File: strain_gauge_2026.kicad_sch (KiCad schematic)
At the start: 0 parts

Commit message: Created Strain Gauge Board Schematic version 1
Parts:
- added C1: 0.1u, Package_SO:SOIC-16_3.9x9.9mm_P1.27mm, symbol Device:C
- added C2, C3, C4, C7, C8: 0.1uF, symbol Device:C
- added C5, C6: 10uF, symbol Device:C
- added J2, J3: Conn_01x04_Socket, Package_DFN_QFN:QFN-20-1EP_5x5mm_P0.65mm_EP3.35x3.35mm, symbol Connector:Conn_01x04_Socket
- added JP1: SolderJumper_2_Open, symbol Jumper:SolderJumper_2_Open
- added L1: 3.3uH, symbol Device:L
- added Q1: S8550, Package_TO_SOT_THT:TO-92_Inline, symbol Transistor_BJT:S8550
- added R1: 10k, symbol Device:R
- added R10, R11, R8, R9: 100, symbol Device:R
- added R12: 20k, Package_TO_SOT_THT:TO-92_Inline, symbol Device:R
- added R13: 8.2k, Package_TO_SOT_THT:TO-92_Inline, symbol Device:R
- added R2, R3, R4, R5, R6, R7: 350, symbol Device:R
- added U1: HX711, Package_SO:SOIC-16_3.9x9.9mm_P1.27mm, symbol Analog_ADC:HX711
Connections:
- new net: C3.2, R11.2, U1.9 (INB-)
- new net: L1.2, Q1.3 (C), R12.1, U1.3 (AVDD)
- new net: R12.2, R13.1, U1.4 (VFB)
- new net: C1.1, U1.6 (VBG)
- new net: JP1.2 (B), R1.2, U1.15 (RATE)
- new net: C3.1, R10.2, U1.10 (INB+)
- new net: C2.2, R9.2, U1.7 (INA-)
- new net: Q1.2 (B), U1.2 (BASE)
- new net: C2.1, R8.2, U1.8 (INA+)
- new net +3V3: C6.1, C7.1, C8.1, J2.1 (Pin_1), Q1.1 (E), R1.1, U1.1 (VSUP), U1.16 (DVDD)
- new net A+: J3.1 (Pin_1), R3.1, R8.1
- new net A-: R2.1, R4.2, R9.1
- new net B+: J3.3 (Pin_3), R10.1, R7.1
- new net B-: R11.1, R5.1, R6.2
- new net Data Out: J2.2 (Pin_2), U1.12 (DOUT)
- new net GND: C1.2, C4.2, C5.2, C6.2, C7.2, C8.2, J2.4 (Pin_4), J3.2 (Pin_2), J3.4 (Pin_4), JP1.1 (A), R13.2, R4.1, R6.1, U1.14 (XI), U1.5 (AGND)
- new net SCK: J2.3 (Pin_3), U1.11 (PD_SCK)
- new net V_AVDD: C4.1, C5.1, L1.1, R2.2, R3.2, R5.2, R7.2
- no-connect marks 0 -> 1
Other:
- note added: "Decoupling caps"
- note added: "Figure out if doing a half bridge - 2 strain resistors on opposite side of beam - R3 and R7 would change to strain resistors - compensates for temperature, and is more sensitive"
- note added: "HX711: https://e2e.ti.com/cfs-file/__key/communityserver-discussions-components-files/73/HX711.pdf SparkFun Board: https://cdn.sparkfun.com/assets/f/5/5/b/c/SparkFun_HX711_Load_Cell.pdf"
- note added: "MCU Connections"
- note added: "Purdue Lunabotics HX711 Strain Gauge Amplifier"
- note added: "RATE is 10 Samples/Sec when grounded, 80 Samples/Sec when pulled up"
- note added: "References Used:"
- note added: "September 26th, 2026"
- note added: "Strain Resistor R_nominal = 350"
- note added: "Strain resistor connections"
- note added: "v1"

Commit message: Fixed ERC errors
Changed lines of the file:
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@@
 	)
 	(junction
-		(at 156.21 151.13)
-		(diameter 0)
-		(color 0 0 0 0)
-	)
-	(junction
 		(at 104.14 92.71)
 		(diameter 0)
@@
 	)
 	(junction
-		(at 162.56 140.97)
-		(diameter 0)
-		(color 0 0 0 0)
-	)
-	(junction
 		(at 104.14 53.34)
 		(diameter 0)
@@
 	)
 	(junction
-		(at 113.03 151.13)
-		(diameter 0)
-		(color 0 0 0 0)
-	)
-	(junction
-		(at 119.38 140.97)
+		(at 104.14 87.63)
 		(diameter 0)
 		(color 0 0 0 0)
 	)
 	(junction
-		(at 104.14 87.63)
+		(at 107.95 50.8)
 		(diameter 0)
 		(color 0 0 0 0)
@@
 	(wire
 		(pts
-			(xy 156.21 151.13) (xy 162.56 151.13)
-		)
-		(stroke
-			(width 0)
-			(type default)
-		)
-	)
-	(wire
-		(pts
 			(xy 99.06 80.01) (xy 104.14 80.01)
 		)
@@
 	(wire
 		(pts
-			(xy 119.38 140.97) (xy 119.38 143.51)
-		)
-		(stroke
-			(width 0)
-			(type default)
-		)
-	)
-	(wire
-		(pts
 			(xy 133.35 58.42) (xy 135.89 58.42)
 		)
@@
 	(wire
 		(pts
-			(xy 113.03 151.13) (xy 119.38 151.13)
-		)
-		(stroke
-			(width 0)
-			(type default)
-		)
-	)
-	(wire
-		(pts
 			(xy 87.63 80.01) (xy 91.44 80.01)
 		)
@@
 	(wire
 		(pts
-			(xy 162.56 140.97) (xy 162.56 143.51)
-		)
-		(stroke
-			(width 0)
-			(type default)
-		)
-	)
-	(wire
-		(pts
 			(xy 104.14 92.71) (xy 120.65 92.71)
 		)
@@
 					(unit 1)
 				)
+			)
+		)
+	)
+	(symbol
+		(lib_id "power:PWR_FLAG")
+		(at 107.95 50.8 270)
+		(unit 1)
+		(body_style 1)
+		(exclude_from_sim no)
+		(in_bom yes)
+		(on_board yes)
+		(in_pos_files yes)
+		(dnp no)
+		(fields_autoplaced yes)
+		(property "Reference" "#FLG01"
+			(at 109.855 50.8 0)
+			(hide yes)
+			(show_name no)
+			(do_not_autoplace no)
+			(effects
+				(font
+					(size 1.27 1.27)
+				)
+			)
+		)
+		(property "Value" "PWR_FLAG"
+			(at 111.76 50.7999 90)
+			(show_name no)
+			(do_not_autoplace no)
+			(effects
+				(font
+					(size 1.27 1.27)
+				)
+				(justify left)
+			)
+		)
+		(property "Footprint" ""
+			(at 107.95 50.8 0)
+			(hide yes)
+			(show_name no)
+			(do_not_autoplace no)
+			(effects
+				(font
+					(size 1.27 1.27)
+				)
+			)
+		)
+		(property "Datasheet" ""
+			(at 107.95 50.8 0)
+			(hide yes)
+			(show_name no)
+			(do_not_autoplace no)
+			(effects
+				(font
+					(size 1.27 1.27)
+				)
+			)
+		)
+		(property "Description" "Special symbol for telling ERC where power comes from"
+			(at 107.95 50.8 0)
+			(hide yes)
+			(show_name no)
+			(do_not_autoplace no)
+			(effects
+				(font
+					(size 1.27 1.27)
+				)
+			)
+		)
+		(pin "1"
+		)
+		(instances
+			(project "strain_gauge_2026"
+				(path "/5a10e1a7-6a1b-4f11-a3d3-893ec92bfd42"
+					(reference "#FLG01")
+					(unit 1)
+				)

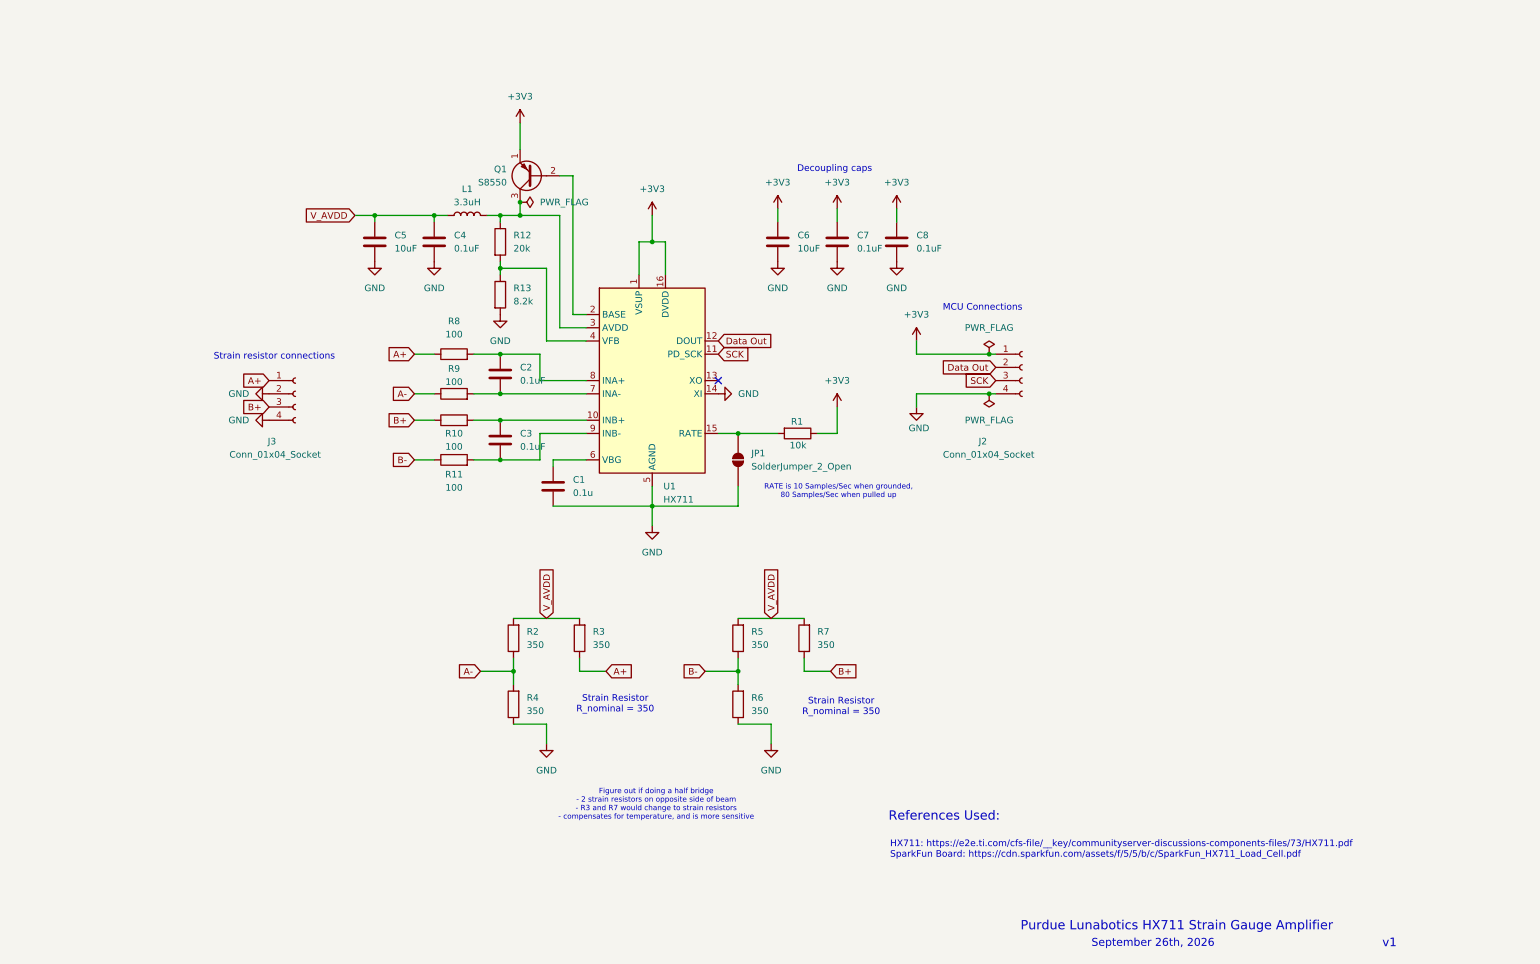
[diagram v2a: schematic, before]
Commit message: New schematic with NAU7802 ADC & LTC4316 I2C Address Translator
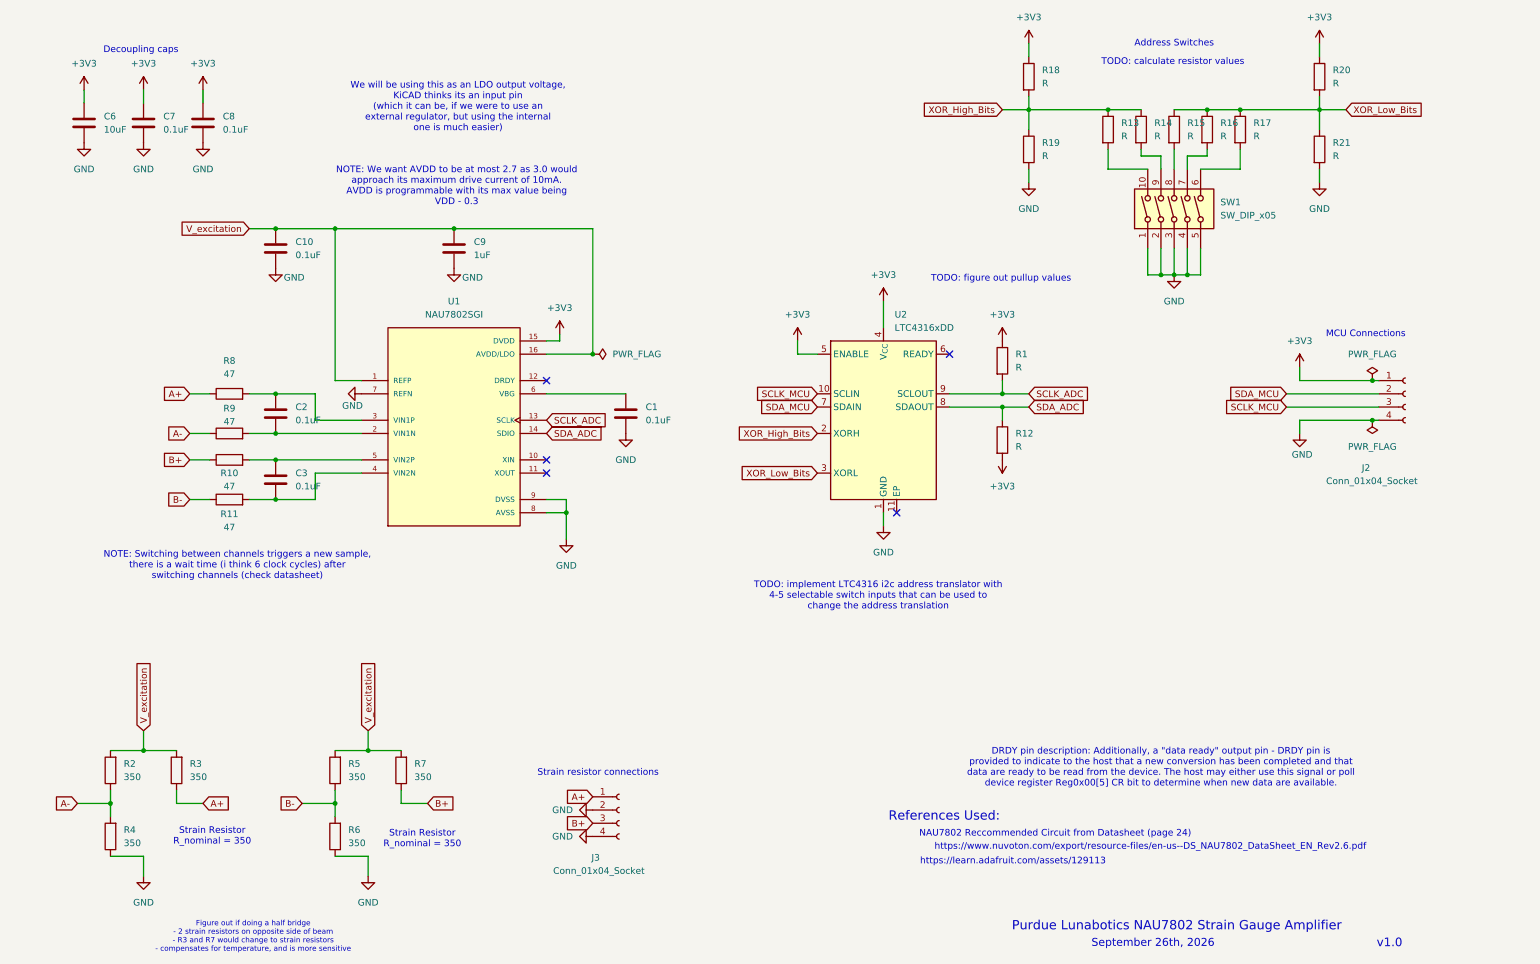
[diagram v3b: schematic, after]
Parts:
- removed C4: 0.1uF, symbol Device:C
- removed C5: 10uF, symbol Device:C
- removed JP1: SolderJumper_2_Open, symbol Jumper:SolderJumper_2_Open
- removed L1: 3.3uH, symbol Device:L
- removed Q1: S8550, Package_TO_SOT_THT:TO-92_Inline, symbol Transistor_BJT:S8550
- removed U1: HX711, Package_SO:SOIC-16_3.9x9.9mm_P1.27mm, symbol Analog_ADC:HX711
- added C10: 0.1uF, symbol Device:C
- added C9: 1uF, symbol Device:C
- added R14, R15, R16, R17, R18, R19, R20, R21: R, symbol Device:R
- added SW1: SW_DIP_x05, Button_Switch_THT:SW_NKK_GW12LJP, symbol Switch:SW_DIP_x05
- added U1: NAU7802SGI, strain_gauge_footprint_lib:SOIC127P600X175-16N, symbol strain_gauge_library:NAU7802SGI
- added U2: LTC4316xDD, Package_DFN_QFN:DFN-10-1EP_3x3mm_P0.5mm_EP1.65x2.38mm, symbol Interface_Expansion:LTC4316xDD
- C1: value 0.1u -> 0.1uF; footprint Package_SO:SOIC-16_3.9x9.9mm_P1.27mm -> (none)
- R1: value 10k -> R
- R10, R11, R8, R9: value 100 -> 47
- R12: value 20k -> R; footprint Package_TO_SOT_THT:TO-92_Inline -> (none)
- R13: value 8.2k -> R; footprint Package_TO_SOT_THT:TO-92_Inline -> (none)
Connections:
- net +3V3: now also R12.2, R18.1, R20.1, U1.15 (DVDD), U2.4 (V_{CC}), U2.5 (ENABLE)
- net GND: now also C10.2, C9.2, R19.2, R21.2, SW1.1, SW1.2, SW1.3, SW1.4, SW1.5, U1.7 (REFN), U1.8 (AVSS), U1.9 (DVSS), U2.1 (GND); no longer R13.2
- net at C3.2, R11.2: now also U1.4 (VIN2N)
- net SDA_ADC: now reaches R12.1
- net SDA_ADC: now also U1.14 (SDIO), U2.8 (SDAOUT)
- net XOR_High_Bits: now reaches R13.1
- net XOR_High_Bits: now also R14.1, R18.2, R19.1, U2.2 (XORH); no longer R12.2
- net at C1.1: now also U1.6 (VBG)
- net SCLK_ADC: now reaches R1.2
- net SCLK_ADC: now also U1.13 (SCLK), U2.9 (SCLOUT)
- net at C3.1, R10.2: now also U1.5 (VIN2P)
- net at C2.2, R9.2: now also U1.2 (VIN1N)
- net at C2.1, R8.2: now also U1.3 (VIN1P)
- net Data Out renamed SDA_MCU
- net SDA_MCU: now also U2.7 (SDAIN)
- net SCK renamed SCLK_MCU
- net SCLK_MCU: now also U2.10 (SCLIN)
- net V_AVDD renamed V_excitation
- net V_excitation: now also C10.1, C9.1, U1.1 (REFP), U1.16 (AVDD/LDO)
- new net: R17.2, SW1.6
- new net: R16.2, SW1.7
- new net: R14.2, SW1.9
- new net: R15.2, SW1.8
- new net: R13.2, SW1.10
- new net XOR_Low_Bits: R15.1, R16.1, R17.1, R20.2, R21.1, U2.3 (XORL)
- no-connect marks 1 -> 5
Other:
- note added: "Address Switches"
- note added: "DRDY pin description: Additionally, a "data ready" output pin - DRDY pin is provided to indicate to the host that a new conversion has been completed and that data are ready to be read from the device. The host may either use this signal or poll device register Reg0x00[5] CR bit to determine when new data are available."
- note added: "NAU7802 Reccommended Circuit from Datasheet (page 24)"
- note added: "NOTE: Switching between channels triggers a new sample, there is a wait time (i think 6 clock cycles) after switching channels (check datasheet)"
- note added: "NOTE: We want AVDD to be at most 2.7 as 3.0 would approach its maximum drive current of 10mA. AVDD is programmable with its max value being VDD - 0.3"
- note added: "Purdue Lunabotics NAU7802 Strain Gauge Amplifier"
- note added: "TODO: calculate resistor values"
- note added: "TODO: figure out pullup values"
- note added: "TODO: implement LTC4316 i2c address translator with 4-5 selectable switch inputs that can be used to change the address translation"
- note added: "We will be using this as an LDO output voltage, KiCAD thinks its an input pin (which it can be, if we were to use an external regulator, but using the internal one is much easier)"
- note added: "https://learn.adafruit.com/assets/129113"
- note added: "https://www.nuvoton.com/export/resource-files/en-us--DS_NAU7802_DataSheet_EN_Rev2.6.pdf"
- note added: "v1.0"
- note removed: "HX711: https://e2e.ti.com/cfs-file/__key/communityserver-discussions-components-files/73/HX711.pdf SparkFun Board: https://cdn.sparkfun.com/assets/f/5/5/b/c/SparkFun_HX711_Load_Cell.pdf"
- note removed: "Purdue Lunabotics HX711 Strain Gauge Amplifier"
- note removed: "RATE is 10 Samples/Sec when grounded, 80 Samples/Sec when pulled up"
- note removed: "v1"
- moved on the sheet: C2, C3, C6, C7, C8, J2, J3, R10, R11, R2, R3, R4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

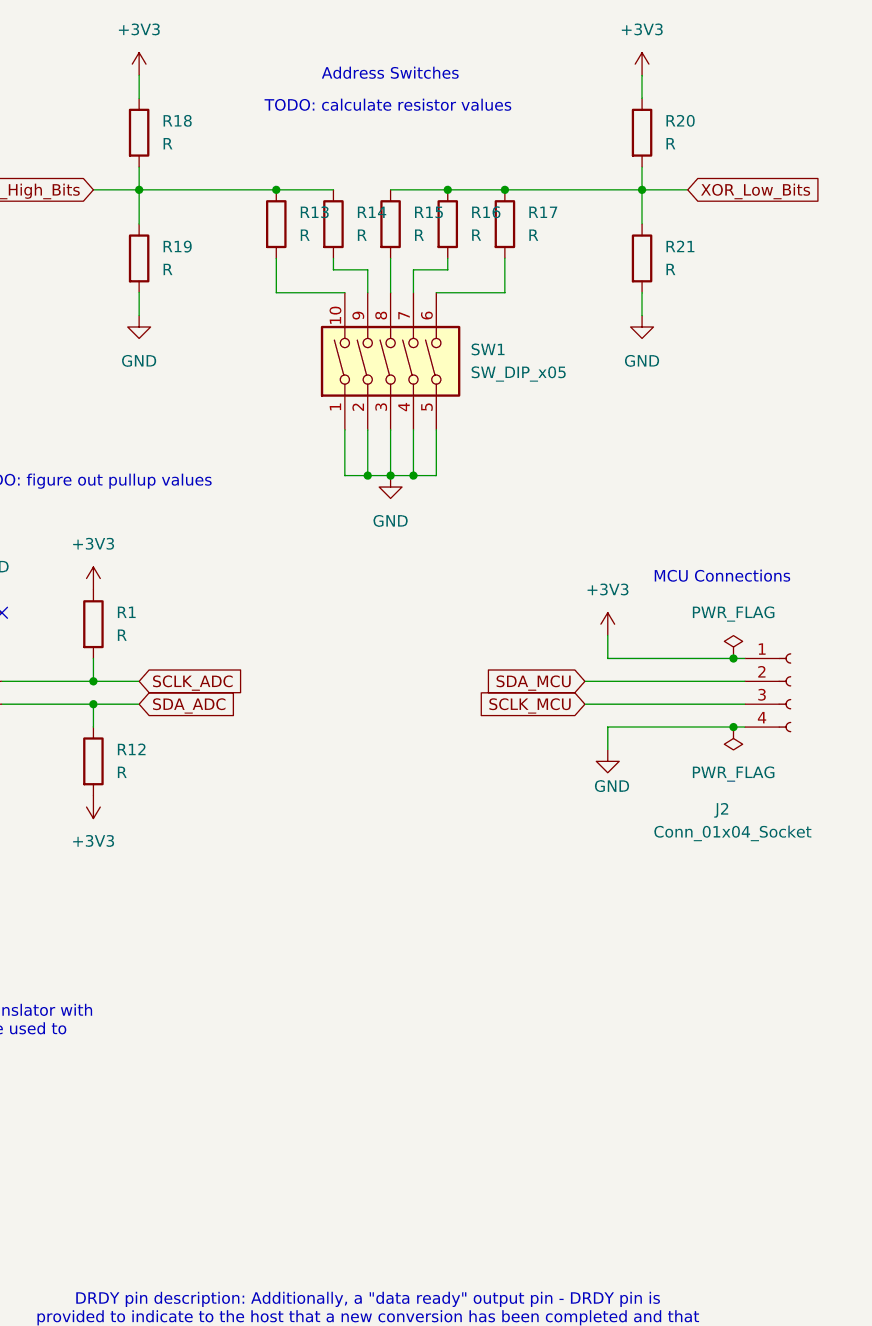
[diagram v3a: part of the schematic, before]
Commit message: Changed to 4-switch Address Selector, Added extra connector to allow for daisy chaining PCBs
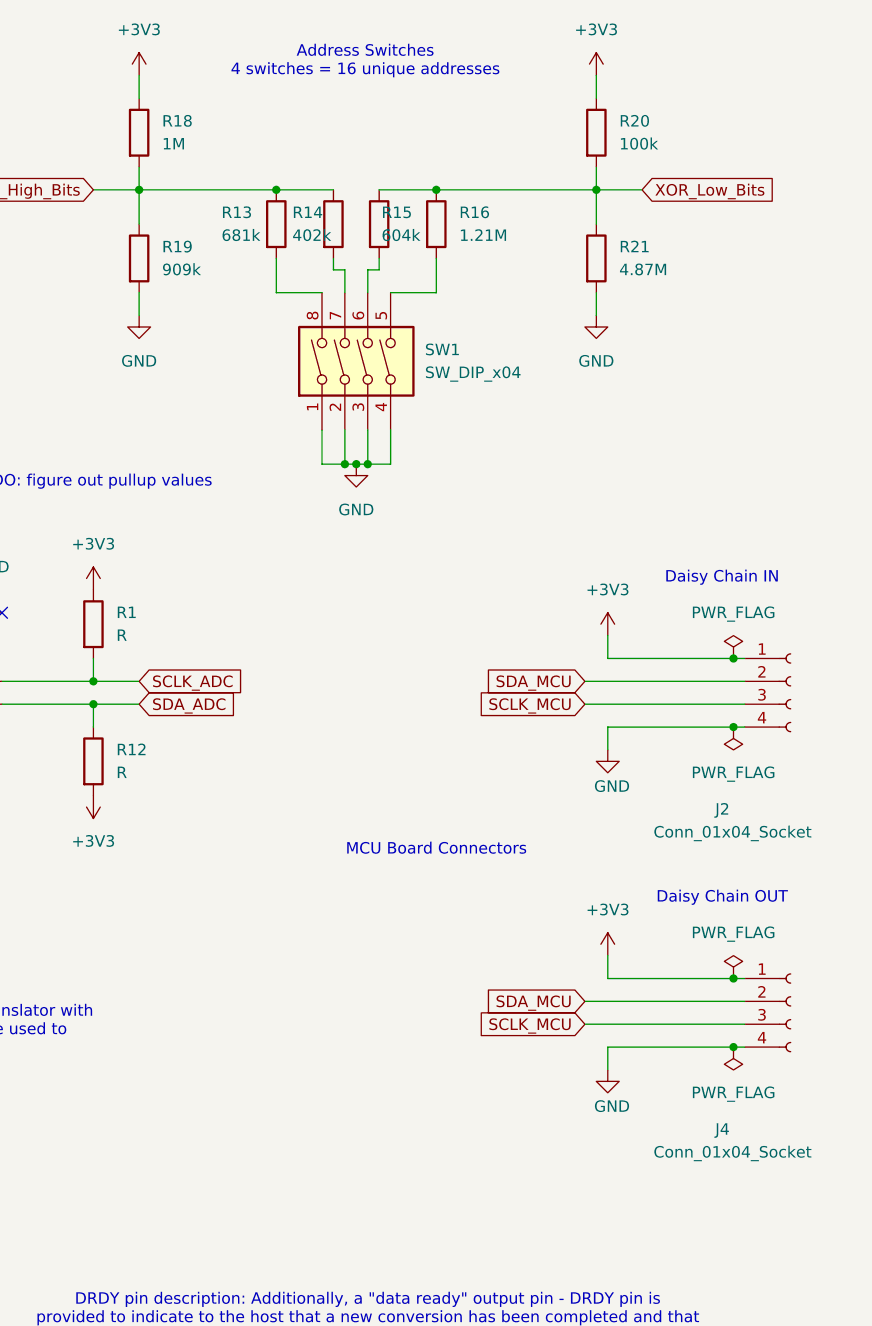
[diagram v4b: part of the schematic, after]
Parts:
- removed R17: R, symbol Device:R
- removed SW1: SW_DIP_x05, Button_Switch_THT:SW_NKK_GW12LJP, symbol Switch:SW_DIP_x05
- added J4: Conn_01x04_Socket, Package_DFN_QFN:QFN-20-1EP_5x5mm_P0.65mm_EP3.35x3.35mm, symbol Connector:Conn_01x04_Socket
- added SW1: SW_DIP_x04, Button_Switch_THT:SW_NKK_GW12LJP, symbol Switch:SW_DIP_x04
- R13: value R -> 681k
- R14: value R -> 402k
- R15: value R -> 604k
- R16: value R -> 1.21M
- R18: value R -> 1M
- R19: value R -> 909k
- R20: value R -> 100k
- R21: value R -> 4.87M
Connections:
- net +3V3: now also J4.1 (Pin_1)
- net GND: now also J4.4 (Pin_4), SW1.1, SW1.2, SW1.3, SW1.4
- net SCLK_MCU: now also J4.3 (Pin_3)
- net SDA_MCU: now also J4.2 (Pin_2)
- net at R16.2: now also SW1.5
- net at R14.2: now also SW1.7
- net at R15.2: now also SW1.6
- net at R13.2: now also SW1.8
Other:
- note added: "Address Switches 4 switches = 16 unique addresses"
- note added: "Daisy Chain IN"
- note added: "Daisy Chain OUT"
- note added: "MCU Board Connectors"
- note removed: "Address Switches"
- note removed: "MCU Connections"
- note removed: "TODO: calculate resistor values"
- moved on the sheet: R15, R16, R20, R21
